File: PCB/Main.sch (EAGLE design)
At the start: 4 parts, among them U1 ESP32DEVKITC

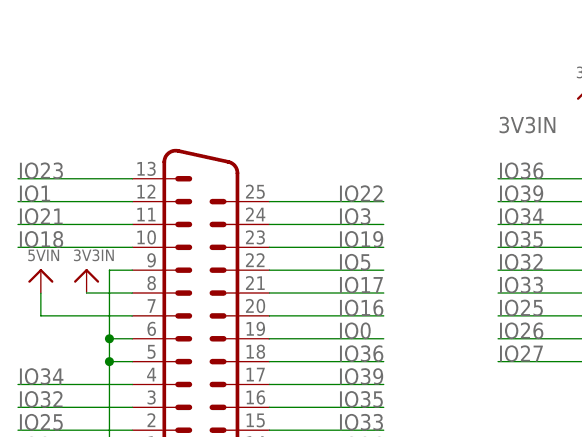
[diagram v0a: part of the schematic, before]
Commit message: Added exposed GND plane at DB25 anchors
All PCBs have been update to have exposed GND plane pads for the DB25 anchor points.

This resolves Issue 54
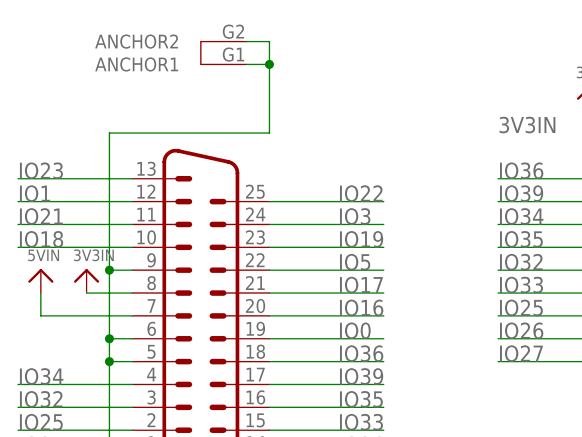
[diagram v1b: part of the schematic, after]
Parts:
- X1: device SparkFun-Retired:DB25_MALEH -> SparkFun-Retired:DB25_MALEHP
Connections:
- net GND: now also X1.ANCHOR1, X1.ANCHOR2
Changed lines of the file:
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@@
 </classes>
 <parts>
-<part name="X1" library="SparkFun-Retired" deviceset="DB25_MALE" device="H"/>
+<part name="X1" library="SparkFun-Retired" deviceset="DB25_MALE" device="HP"/>
 <part name="U$25" library="Airquality_Sensor" library_urn="urn:adsk.eagle:library:16015176" deviceset="GND" device=""/>
 <part name="U$27" library="microbuilder" deviceset="VIN" device="" value="5VIN"/>
@@
 <wire x1="233.68" y1="-12.7" x2="231.14" y2="-12.7" width="0.1524" layer="91"/>
 <junction x="231.14" y="-12.7"/>
+<wire x1="231.14" y1="-2.54" x2="231.14" y2="12.7" width="0.1524" layer="91"/>
+<junction x="231.14" y="-2.54"/>
+<wire x1="231.14" y1="12.7" x2="248.92" y2="12.7" width="0.1524" layer="91"/>
+<wire x1="248.92" y1="12.7" x2="248.92" y2="20.32" width="0.1524" layer="91"/>
+<pinref part="X1" gate="-1" pin="ANCHOR2"/>
+<wire x1="248.92" y1="20.32" x2="248.92" y2="22.86" width="0.1524" layer="91"/>
+<wire x1="248.92" y1="22.86" x2="246.38" y2="22.86" width="0.1524" layer="91"/>
+<pinref part="X1" gate="-1" pin="ANCHOR1"/>
+<wire x1="246.38" y1="20.32" x2="248.92" y2="20.32" width="0.1524" layer="91"/>
+<junction x="248.92" y="20.32"/>
 </segment>
 <segment>

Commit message: Retiring Main PCB
Retiring Original Main PCB design as the unit is thinner that the standard footprint.  This was causing  confusion.  The new main used to be Main Alt Wide version.  It is now the standard as it fits the standard ESP footprint.  The Thinner version has been moved to the retired folder in PCBs
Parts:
- U1: device ESP32-DEVKITC:ESP32DEVKITC -> ESP32-DEVKITC4:ESP32DEVKITC
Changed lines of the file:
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@@
 <layers>
 <layer number="1" name="Top" color="4" fill="1" visible="no" active="no"/>
-<layer number="2" name="Route2" color="1" fill="3" visible="no" active="no"/>
-<layer number="15" name="Route15" color="4" fill="6" visible="no" active="no"/>
+<layer number="2" name="Route2" color="16" fill="1" visible="no" active="no"/>
+<layer number="15" name="Route15" color="23" fill="1" visible="no" active="no"/>
 <layer number="16" name="Bottom" color="1" fill="1" visible="no" active="no"/>
 <layer number="17" name="Pads" color="2" fill="1" visible="no" active="no"/>
@@
 <part name="U$27" library="microbuilder" deviceset="VIN" device="" value="5VIN"/>
 <part name="U$28" library="microbuilder" deviceset="VIN" device="" value="3V3IN"/>
-<part name="U1" library="ESP32-DEVKITC" deviceset="ESP32DEVKITC" device=""/>
 <part name="U$26" library="Airquality_Sensor" library_urn="urn:adsk.eagle:library:16015176" deviceset="GND" device=""/>
 <part name="U$29" library="Airquality_Sensor" library_urn="urn:adsk.eagle:library:16015176" deviceset="GND" device=""/>
@@
 <part name="U$32" library="microbuilder" deviceset="VIN" device="" value="3V3IN"/>
 <part name="U$33" library="Airquality_Sensor" library_urn="urn:adsk.eagle:library:16015176" deviceset="GND" device=""/>
+<part name="U1" library="ESP32-DEVKITC4" deviceset="ESP32DEVKITC" device=""/>
 </parts>
 <sheets>
@@
 <attribute name="VALUE" x="227.076" y="-1.524" size="1.27" layer="96"/>
 </instance>
-<instance part="U1" gate="G$1" x="304.8" y="-10.16" smashed="yes" rot="R270">
-<attribute name="NAME" x="309.88" y="16.51" size="1.27" layer="95"/>
-</instance>
 <instance part="U$26" gate="G$1" x="325.12" y="-40.64" smashed="yes">
 <attribute name="VALUE" x="323.596" y="-43.18" size="1.27" layer="96"/>
@@
 <instance part="U$33" gate="G$1" x="350.52" y="-27.94" smashed="yes">
 <attribute name="VALUE" x="348.996" y="-30.48" size="1.27" layer="96"/>
+</instance>
+<instance part="U1" gate="G$1" x="304.8" y="-10.16" smashed="yes" rot="R270">
+<attribute name="NAME" x="309.88" y="16.51" size="1.27" layer="95"/>
 </instance>
 </instances>
@@
 <junction x="231.14" y="-2.54"/>
 <wire x1="231.14" y1="12.7" x2="248.92" y2="12.7" width="0.1524" layer="91"/>
+<pinref part="X1" gate="-1" pin="ANCHOR2"/>
 <wire x1="248.92" y1="12.7" x2="248.92" y2="20.32" width="0.1524" layer="91"/>
-<pinref part="X1" gate="-1" pin="ANCHOR2"/>
 <wire x1="248.92" y1="20.32" x2="248.92" y2="22.86" width="0.1524" layer="91"/>
 <wire x1="248.92" y1="22.86" x2="246.38" y2="22.86" width="0.1524" layer="91"/>
@@
 </segment>
 <segment>
-<pinref part="U1" gate="G$1" pin="GND@38"/>
 <wire x1="322.58" y1="12.7" x2="325.12" y2="12.7" width="0.1524" layer="91"/>
 <wire x1="325.12" y1="12.7" x2="325.12" y2="-2.54" width="0.1524" layer="91"/>
-<pinref part="U1" gate="G$1" pin="GND@32"/>
 <wire x1="325.12" y1="-2.54" x2="325.12" y2="-38.1" width="0.1524" layer="91"/>
 <wire x1="322.58" y1="-2.54" x2="325.12" y2="-2.54" width="0.1524" layer="91"/>
 <junction x="325.12" y="-2.54"/>
 <pinref part="U$26" gate="G$1" pin="GND"/>
-</segment>
-<segment>
-<pinref part="U1" gate="G$1" pin="GND@14"/>
+<pinref part="U1" gate="G$1" pin="GND@32"/>
+<pinref part="U1" gate="G$1" pin="GND@38"/>
+</segment>
+<segment>
 <wire x1="287.02" y1="-20.32" x2="284.48" y2="-20.32" width="0.1524" layer="91"/>
 <wire x1="284.48" y1="-20.32" x2="284.48" y2="-35.56" width="0.1524" layer="91"/>
 <pinref part="U$29" gate="G$1" pin="GND"/>
+<pinref part="U1" gate="G$1" pin="GND@14"/>
 </segment>
 <segment>
@@
 </segment>
 <segment>
-<pinref part="U1" gate="G$1" pin="5V"/>
 <wire x1="287.02" y1="-33.02" x2="279.4" y2="-33.02" width="0.1524" layer="91"/>
 <wire x1="279.4" y1="-33.02" x2="279.4" y2="-30.48" width="0.1524" layer="91"/>
 <pinref part="U$30" gate="G$1" pin="VIN"/>
 <label x="271.78" y="-33.02" size="1.778" layer="95"/>
+<pinref part="U1" gate="G$1" pin="5V"/>
 </segment>
 </net>
@@
 </segment>
 <segment>
-<pinref part="U1" gate="G$1" pin="3V3"/>
 <wire x1="287.02" y1="12.7" x2="284.48" y2="12.7" width="0.1524" layer="91"/>
 <wire x1="284.48" y1="12.7" x2="284.48" y2="15.24" width="0.1524" layer="91"/>
 <pinref part="U$31" gate="G$1" pin="VIN"/>
 <label x="274.32" y="12.7" size="1.778" layer="95"/>
+<pinref part="U1" gate="G$1" pin="3V3"/>
 </segment>
 </net>
@@
 </segment>
 <segment>
-<pinref part="U1" gate="G$1" pin="IO5"/>
 <wire x1="322.58" y1="-10.16" x2="335.28" y2="-10.16" width="0.1524" layer="91"/>
 <label x="330.2" y="-10.16" size="1.778" layer="95"/>
+<pinref part="U1" gate="G$1" pin="IO5"/>
 </segment>
 </net>
@@
 </segment>
 <segment>
-<pinref part="U1" gate="G$1" pin="IO18"/>
 <wire x1="322.58" y1="-7.62" x2="335.28" y2="-7.62" width="0.1524" layer="91"/>
 <label x="330.2" y="-7.62" size="1.778" layer="95"/>
+<pinref part="U1" gate="G$1" pin="IO18"/>
 </segment>
 </net>
@@
 </segment>
 <segment>
-<pinref part="U1" gate="G$1" pin="IO23"/>
 <wire x1="322.58" y1="10.16" x2="335.28" y2="10.16" width="0.1524" layer="91"/>
 <label x="330.2" y="10.16" size="1.778" layer="95"/>
+<pinref part="U1" gate="G$1" pin="IO23"/>
 </segment>
 </net>
@@
 </segment>
 <segment>
-<pinref part="U1" gate="G$1" pin="RXD0"/>
 <wire x1="322.58" y1="2.54" x2="335.28" y2="2.54" width="0.1524" layer="91"/>
 <label x="330.2" y="2.54" size="1.778" layer="95"/>
+<pinref part="U1" gate="G$1" pin="RXD0"/>
 </segment>
 </net>
@@
 </segment>
 <segment>
-<pinref part="U1" gate="G$1" pin="IO26"/>
 <wire x1="287.02" y1="-10.16" x2="274.32" y2="-10.16" width="0.1524" layer="91"/>
 <label x="274.32" y="-10.16" size="1.778" layer="95"/>
+<pinref part="U1" gate="G$1" pin="IO26"/>
 </segment>
 </net>
@@
 </segment>
 <segment>
-<pinref part="U1" gate="G$1" pin="IO33"/>
 <wire x1="287.02" y1="-5.08" x2="274.32" y2="-5.08" width="0.1524" layer="91"/>
 <label x="274.32" y="-5.08" size="1.778" layer="95"/>
+<pinref part="U1" gate="G$1" pin="IO33"/>
 </segment>
 </net>
@@
 </segment>
 <segment>
-<pinref part="U1" gate="G$1" pin="TXD0"/>
 <wire x1="322.58" y1="5.08" x2="335.28" y2="5.08" width="0.1524" layer="91"/>
 <label x="330.2" y="5.08" size="1.778" layer="95"/>
+<pinref part="U1" gate="G$1" pin="TXD0"/>
 </segment>
 </net>
@@
 </segment>
 <segment>
-<pinref part="U1" gate="G$1" pin="IO21"/>
 <wire x1="322.58" y1="0" x2="335.28" y2="0" width="0.1524" layer="91"/>
 <label x="330.2" y="0" size="1.778" layer="95"/>
+<pinref part="U1" gate="G$1" pin="IO21"/>
 </segment>
 </net>
@@
 </segment>
 <segment>
-<pinref part="U1" gate="G$1" pin="IO34"/>
 <wire x1="287.02" y1="2.54" x2="274.32" y2="2.54" width="0.1524" layer="91"/>
 <label x="274.32" y="2.54" size="1.778" layer="95"/>
+<pinref part="U1" gate="G$1" pin="IO34"/>
 </segment>
 </net>
@@
 </segment>
 <segment>
-<pinref part="U1" gate="G$1" pin="IO32"/>
 <wire x1="287.02" y1="-2.54" x2="274.32" y2="-2.54" width="0.1524" layer="91"/>
 <label x="274.32" y="-2.54" size="1.778" layer="95"/>
+<pinref part="U1" gate="G$1" pin="IO32"/>
 </segment>
 </net>
@@
 </segment>
 <segment>
-<pinref part="U1" gate="G$1" pin="IO25"/>
 <wire x1="287.02" y1="-7.62" x2="274.32" y2="-7.62" width="0.1524" layer="91"/>
 <label x="274.32" y="-7.62" size="1.778" layer="95"/>
+<pinref part="U1" gate="G$1" pin="IO25"/>
 </segment>
 </net>
@@
 </segment>
 <segment>
-<pinref part="U1" gate="G$1" pin="IO27"/>
 <wire x1="287.02" y1="-12.7" x2="274.32" y2="-12.7" width="0.1524" layer="91"/>
 <label x="274.32" y="-12.7" size="1.778" layer="95"/>
+<pinref part="U1" gate="G$1" pin="IO27"/>
 </segment>
 </net>
@@
 </segment>
 <segment>
-<pinref part="U1" gate="G$1" pin="IO35"/>
 <wire x1="287.02" y1="0" x2="274.32" y2="0" width="0.1524" layer="91"/>
 <label x="274.32" y="0" size="1.778" layer="95"/>
+<pinref part="U1" gate="G$1" pin="IO35"/>
 </segment>
 </net>
@@
 </segment>
 <segment>
-<pinref part="U1" gate="G$1" pin="SVN"/>
 <wire x1="287.02" y1="5.08" x2="274.32" y2="5.08" width="0.1524" layer="91"/>
 <label x="274.32" y="5.08" size="1.778" layer="95"/>
+<pinref part="U1" gate="G$1" pin="SVN"/>
 </segment>
 </net>
@@
 </segment>
 <segment>
-<pinref part="U1" gate="G$1" pin="IO0"/>
 <wire x1="322.58" y1="-20.32" x2="335.28" y2="-20.32" width="0.1524" layer="91"/>
 <label x="330.2" y="-20.32" size="1.778" layer="95"/>
+<pinref part="U1" gate="G$1" pin="IO0"/>
 </segment>
 </net>
@@
 </segment>
 <segment>
-<pinref part="U1" gate="G$1" pin="IO16"/>
 <wire x1="322.58" y1="-15.24" x2="335.28" y2="-15.24" width="0.1524" layer="91"/>
 <label x="330.2" y="-15.24" size="1.778" layer="95"/>
+<pinref part="U1" gate="G$1" pin="IO16"/>
 </segment>
 </net>
@@
 </segment>
 <segment>
-<pinref part="U1" gate="G$1" pin="IO17"/>
 <wire x1="322.58" y1="-12.7" x2="335.28" y2="-12.7" width="0.1524" layer="91"/>
 <label x="330.2" y="-12.7" size="1.778" layer="95"/>
+<pinref part="U1" gate="G$1" pin="IO17"/>
 </segment>
 <segment>
@@
 </segment>
 <segment>
-<pinref part="U1" gate="G$1" pin="IO19"/>
 <wire x1="322.58" y1="-5.08" x2="335.28" y2="-5.08" width="0.1524" layer="91"/>
 <label x="330.2" y="-5.08" size="1.778" layer="95"/>
+<pinref part="U1" gate="G$1" pin="IO19"/>
 </segment>
 </net>
@@
 </segment>
 <segment>
-<pinref part="U1" gate="G$1" pin="IO22"/>
 <wire x1="322.58" y1="7.62" x2="335.28" y2="7.62" width="0.1524" layer="91"/>
 <label x="330.2" y="7.62" size="1.778" layer="95"/>
+<pinref part="U1" gate="G$1" pin="IO22"/>
 </segment>
 </net>
 <net name="IO36" class="0">
 <segment>
-<pinref part="U1" gate="G$1" pin="SVP"/>
 <wire x1="287.02" y1="7.62" x2="274.32" y2="7.62" width="0.1524" layer="91"/>
 <label x="274.32" y="7.62" size="1.778" layer="95"/>
+<pinref part="U1" gate="G$1" pin="SVP"/>
 </segment>
 <segment>
@@
 </sheet>
 </sheets>
+<errors>
+</errors>
 </schematic>
 </drawing>
